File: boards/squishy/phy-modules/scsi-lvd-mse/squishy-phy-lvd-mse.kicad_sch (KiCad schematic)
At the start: 14 parts, among them J1 SCSI PHY Mezz, J2 SCSI Connector, U1 M24C02-RMC

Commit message: squishy: phy: updated the pinout to the connector module to allow for +3v3 so we can power the ID chip on the board
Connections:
- net +3V3: now also J2.3 (Pin_3)
- no-connect marks 19 -> 18

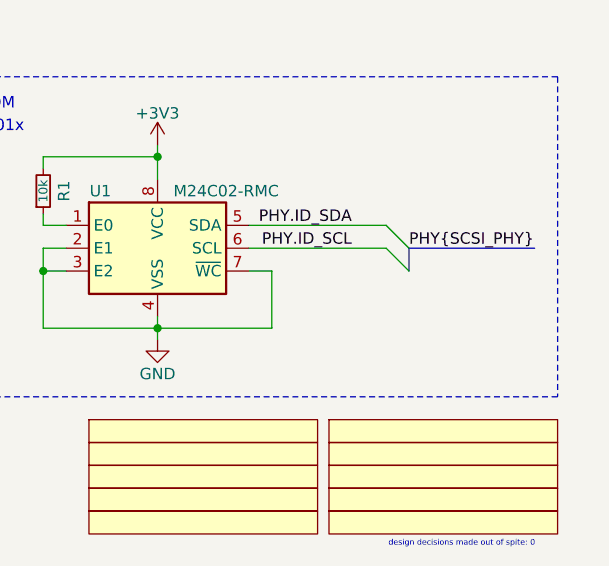
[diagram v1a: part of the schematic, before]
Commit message: squishy: phy: Added debug/programming connector for the PHY EEPROMs
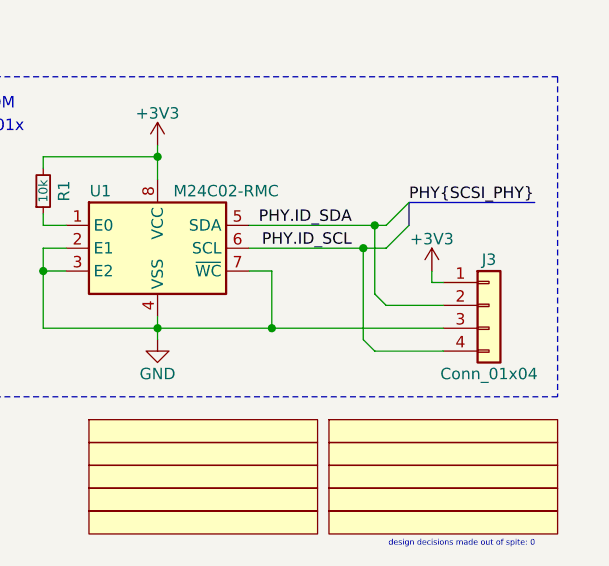
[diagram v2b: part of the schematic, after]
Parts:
- added J3: Conn_01x04, pkl_connectors_wuerth:490107670412-d, symbol Connector_Generic:Conn_01x04
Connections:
- net +3V3: now also J3.1 (Pin_1)
- net GND: now also J3.3 (Pin_3)
- net PHY.ID_SCL: now also J3.4 (Pin_4)
- net PHY.ID_SDA: now also J3.2 (Pin_2)
